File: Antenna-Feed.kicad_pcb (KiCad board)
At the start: 2 copper layers, 26 x 17.2 mm, 3 parts, among them J1 SMA, J2 SMA, J3 SMA

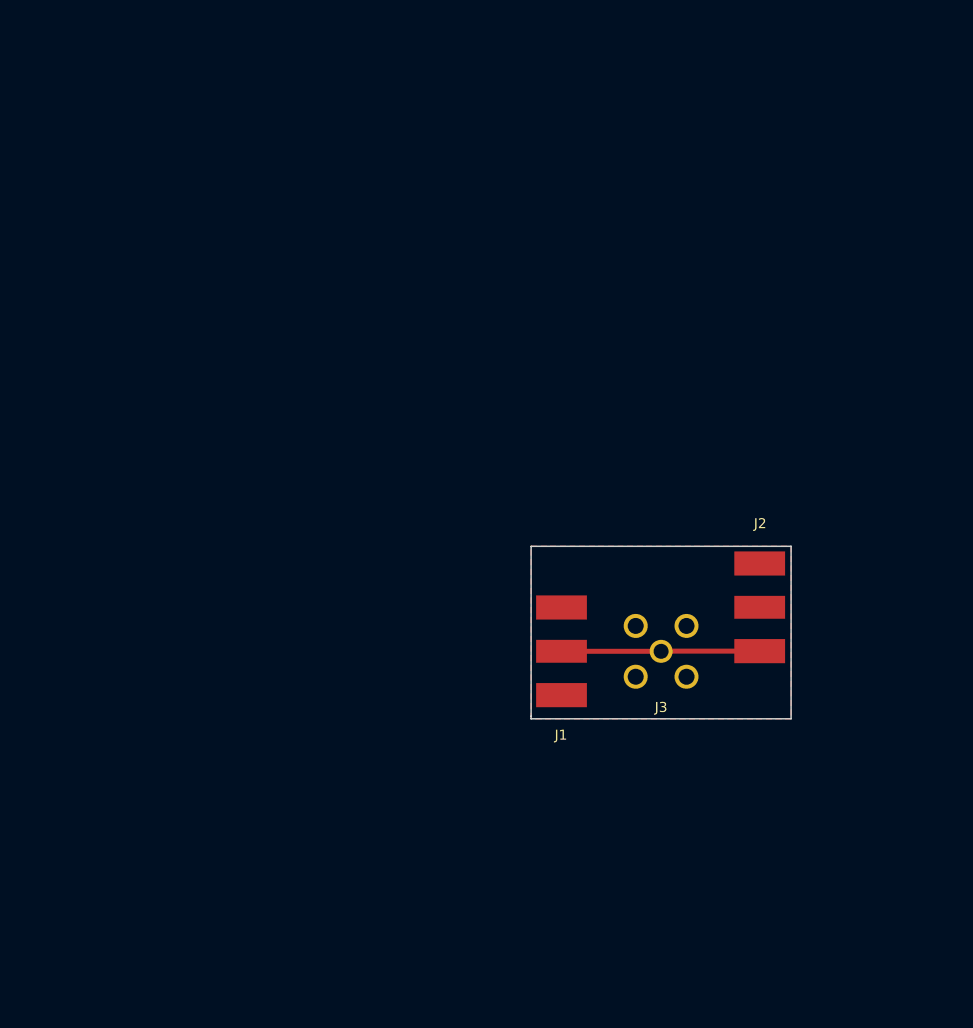
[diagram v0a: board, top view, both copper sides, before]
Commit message: initial revision conforming to Ana's structural model
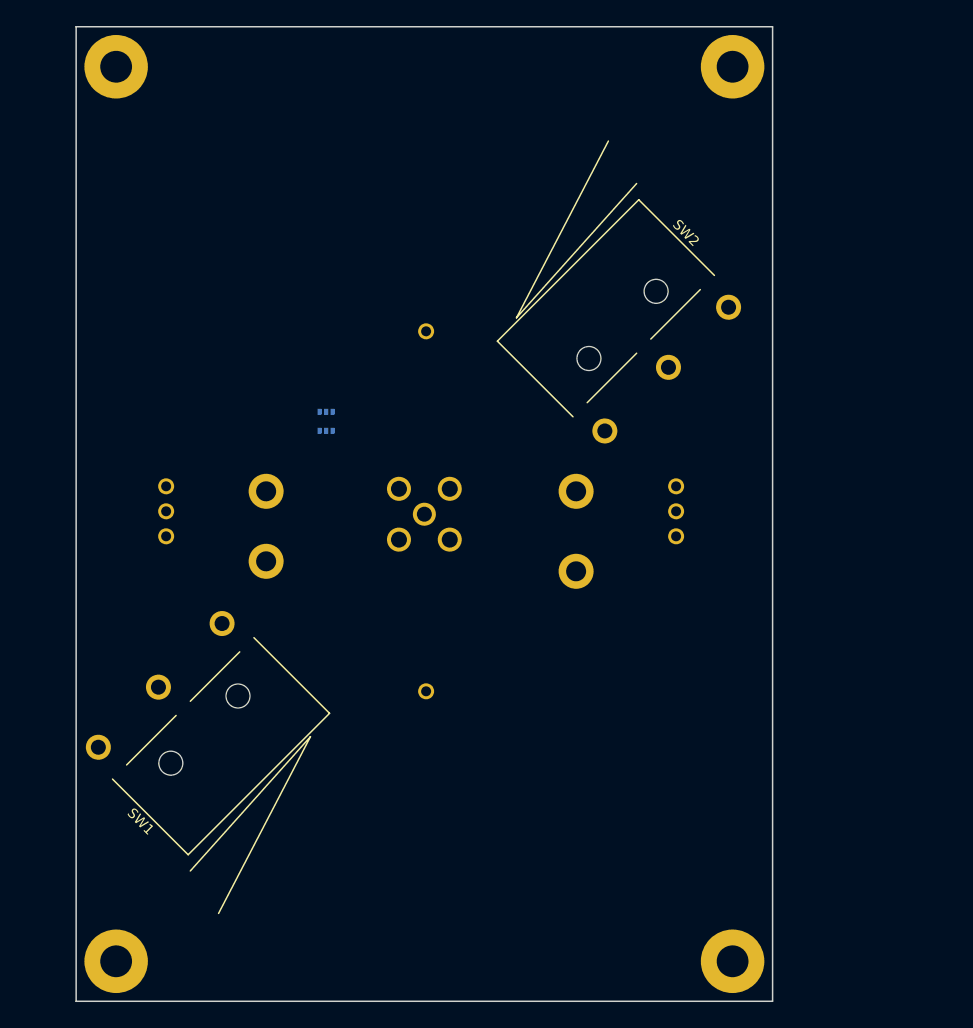
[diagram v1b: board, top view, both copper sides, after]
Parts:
- added J10: PC104PTH, SFUSat:PC104PTH, F.Cu at (155.7, 136.0)
- added J11: PC104PTH, SFUSat:PC104PTH, F.Cu at (94.0, 136.0)
- added J12: PC104PTH, SFUSat:PC104PTH, F.Cu at (94.0, 46.5)
- added J13: PC104PTH, SFUSat:PC104PTH, F.Cu at (155.7, 46.5)
- added J4: Conn_01x01, SFUSat:via-0.97mm, F.Cu at (125.0, 73.0)
- added J5: Conn_01x01, SFUSat:PTH-2.0mm, F.Cu at (109.0, 96.0)
- added J6: Conn_01x01, SFUSat:PTH-2.0mm, F.Cu at (109.0, 89.0)
- added J7: Conn_01x01, SFUSat:PTH-2.0mm, F.Cu at (140.0, 97.0)
- added J8: Conn_01x01, SFUSat:PTH-2.0mm, F.Cu at (140.0, 89.0)
- added J9: B3B-XH-A(LF)(SN), SFUSat:B3B-XH-A, B.Cu at (150.0, 91.0)
- added SW1: LIMIT_SWITCH, SFUSat:SS-3GLPD-R, F.Cu at (100.0, 110.0)
- added SW2: LIMIT_SWITCH, SFUSat:SS-3GLPD-R, F.Cu at (147.5, 75.2)
- added U1: NC7SZ157, SFUSat:SOT-363, B.Cu at (115.0, 82.0)
- J1: value SMA -> Conn_01x01; footprint SFUSat:SMA_EDGE -> SFUSat:via-0.97mm
- J2: value SMA -> B3B-XH-A(LF)(SN); footprint SFUSat:SMA_EDGE -> SFUSat:B3B-XH-A; moved to B.Cu
- J3: moved to B.Cu
- moved J2 62.6 mm to (99.0, 91.0), turned to 90 degrees
- moved J3 27.4 mm to (124.8, 91.3)
- moved J1 11.7 mm to (125.0, 109.0)
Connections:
- J2 pad 1: Net-(J1-Pad2) -> Net-(J2-Pad1)
- J2 pad 2: Net-(J1-Pad1) -> Net-(J2-Pad2)
- J3 pad 2: Net-(J1-Pad2) -> Net-(J3-Pad2)
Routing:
- net Net-(J1-Pad1): track 19.8 -> 0.00 mm
- removed copper zone on F.Cu, net Net-(J1-Pad2)
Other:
- board size 26 x 17.2 mm -> 69.7 x 97.5 mm

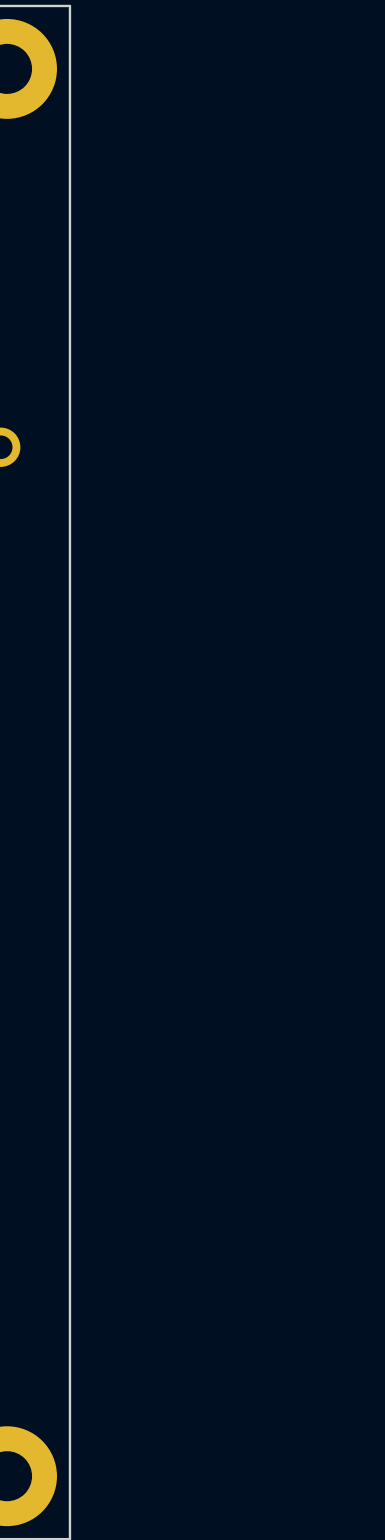
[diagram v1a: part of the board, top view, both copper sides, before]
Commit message: Added through holes to the right side of the antenna feed pcb
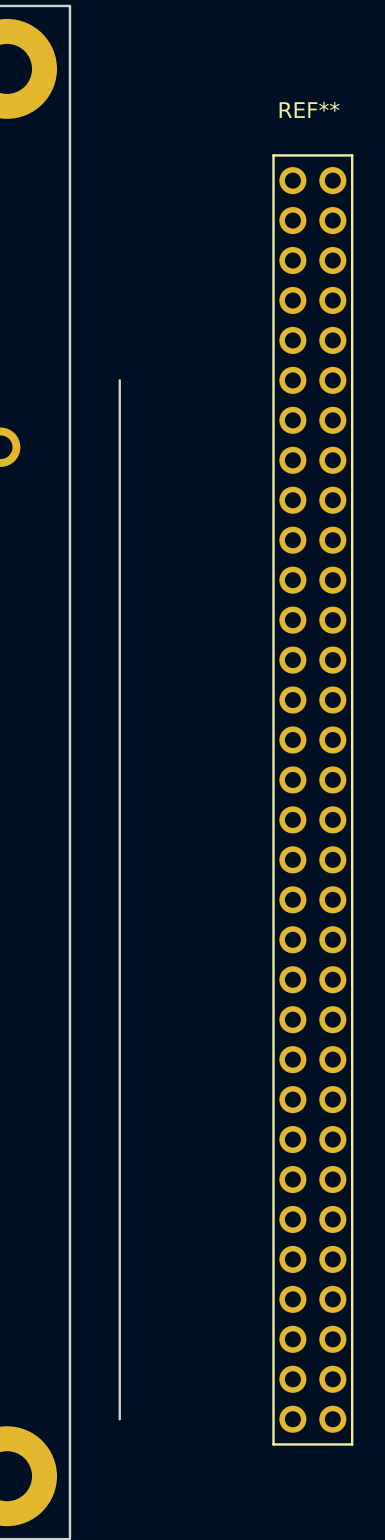
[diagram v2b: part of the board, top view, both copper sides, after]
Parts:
- added REF**: PC104-8bit, SFUSat:PC104-8bit, F.Cu at (175.1, 93.0)
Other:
- board size 69.7 x 97.5 mm -> 72.8 x 97.5 mm
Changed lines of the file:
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@@
-(kicad_pcb (version 4) (host pcbnew 4.0.7-e2-6376~58~ubuntu16.04.1)
+(kicad_pcb (version 4) (host pcbnew 4.0.7)
   (general
-    (links 17)
+    (links 0)
     (no_connects 17)
-    (area 89.924999 42.464999 159.725001 140.075001)
+    (area 80.650001 41.755 159.725001 144.700001)
     (thickness 1.6)
-    (drawings 6)
+    (drawings 7)
     (tracks 0)
     (zones 0)
-    (modules 16)
+    (modules 17)
     (nets 17)
   )
@@
       (net 7 "Net-(J9-Pad2)"))
   )
+  (module SFUSat:PC104-8bit (layer F.Cu)
+    (at 175.09 93.01)
+    (fp_text reference REF** (at -0.254 -43.815) (layer F.SilkS)
+      (effects (font (size 1 1) (thickness 0.15)))
+    )
+    (fp_text value PC104-8bit (at -0.127 -42.164) (layer F.Fab)
+      (effects (font (size 1 1) (thickness 0.15)))
+    )
+    (fp_line (start -2.5 40.97) (end 2.5 40.97) (layer F.SilkS) (width 0.15))
+    (fp_line (start -2.5 -40.97) (end -2.5 40.97) (layer F.SilkS) (width 0.15))
+    (fp_line (start 2.5 -40.97) (end 2.5 40.97) (layer F.SilkS) (width 0.15))
+    (fp_line (start -2.5 -40.97) (end 2.5 -40.97) (layer F.SilkS) (width 0.15))
+    (pad 32B thru_hole circle (at -1.27 -39.37) (size 1.72 1.72) (drill 1.02) (layers *.Cu *.Mask))
+    (pad 31B thru_hole circle (at -1.27 -36.83) (size 1.72 1.72) (drill 1.02) (layers *.Cu *.Mask))
+    (pad 30B thru_hole circle (at -1.27 -34.29) (size 1.72 1.72) (drill 1.02) (layers *.Cu *.Mask))
+    (pad 29B thru_hole circle (at -1.27 -31.75) (size 1.72 1.72) (drill 1.02) (layers *.Cu *.Mask))
+    (pad 28B thru_hole circle (at -1.27 -29.21) (size 1.72 1.72) (drill 1.02) (layers *.Cu *.Mask))
+    (pad 27B thru_hole circle (at -1.27 -26.67) (size 1.72 1.72) (drill 1.02) (layers *.Cu *.Mask))
+    (pad 26B thru_hole circle (at -1.27 -24.13) (size 1.72 1.72) (drill 1.02) (layers *.Cu *.Mask))
+    (pad 25B thru_hole circle (at -1.27 -21.59) (size 1.72 1.72) (drill 1.02) (layers *.Cu *.Mask))
+    (pad 24B thru_hole circle (at -1.27 -19.05) (size 1.72 1.72) (drill 1.02) (layers *.Cu *.Mask))
+    (pad 23B thru_hole circle (at -1.27 -16.51) (size 1.72 1.72) (drill 1.02) (layers *.Cu *.Mask))
+    (pad 22B thru_hole circle (at -1.27 -13.97) (size 1.72 1.72) (drill 1.02) (layers *.Cu *.Mask))
+    (pad 21B thru_hole circle (at -1.27 -11.43) (size 1.72 1.72) (drill 1.02) (layers *.Cu *.Mask))
+    (pad 20B thru_hole circle (at -1.27 -8.89) (size 1.72 1.72) (drill 1.02) (layers *.Cu *.Mask))
+    (pad 19B thru_hole circle (at -1.27 -6.35) (size 1.72 1.72) (drill 1.02) (layers *.Cu *.Mask))
+    (pad 18B thru_hole circle (at -1.27 -3.81) (size 1.72 1.72) (drill 1.02) (layers *.Cu *.Mask))
+    (pad 17B thru_hole circle (at -1.27 -1.27) (size 1.72 1.72) (drill 1.02) (layers *.Cu *.Mask))
+    (pad 16B thru_hole circle (at -1.27 1.27) (size 1.72 1.72) (drill 1.02) (layers *.Cu *.Mask))
+    (pad 15B thru_hole circle (at -1.27 3.81) (size 1.72 1.72) (drill 1.02) (layers *.Cu *.Mask))
+    (pad 14B thru_hole circle (at -1.27 6.35) (size 1.72 1.72) (drill 1.02) (layers *.Cu *.Mask))
+    (pad 13B thru_hole circle (at -1.27 8.89) (size 1.72 1.72) (drill 1.02) (layers *.Cu *.Mask))
+    (pad 12B thru_hole circle (at -1.27 11.43) (size 1.72 1.72) (drill 1.02) (layers *.Cu *.Mask))
+    (pad 11B thru_hole circle (at -1.27 13.97) (size 1.72 1.72) (drill 1.02) (layers *.Cu *.Mask))
+    (pad 10B thru_hole circle (at -1.27 16.51) (size 1.72 1.72) (drill 1.02) (layers *.Cu *.Mask))
+    (pad 9B thru_hole circle (at -1.27 19.05) (size 1.72 1.72) (drill 1.02) (layers *.Cu *.Mask))
+    (pad 8B thru_hole circle (at -1.27 21.59) (size 1.72 1.72) (drill 1.02) (layers *.Cu *.Mask))
+    (pad 7B thru_hole circle (at -1.27 24.13) (size 1.72 1.72) (drill 1.02) (layers *.Cu *.Mask))
+    (pad 6B thru_hole circle (at -1.27 26.67) (size 1.72 1.72) (drill 1.02) (layers *.Cu *.Mask))
+    (pad 5B thru_hole circle (at -1.27 29.21) (size 1.72 1.72) (drill 1.02) (layers *.Cu *.Mask))
+    (pad 4B thru_hole circle (at -1.27 31.75) (size 1.72 1.72) (drill 1.02) (layers *.Cu *.Mask))
+    (pad 3B thru_hole circle (at -1.27 34.29) (size 1.72 1.72) (drill 1.02) (layers *.Cu *.Mask))
+    (pad 2B thru_hole circle (at -1.27 36.83) (size 1.72 1.72) (drill 1.02) (layers *.Cu *.Mask))
+    (pad 1B thru_hole circle (at -1.27 39.37) (size 1.72 1.72) (drill 1.02) (layers *.Cu *.Mask))
+    (pad 32A thru_hole circle (at 1.27 -39.37) (size 1.72 1.72) (drill 1.02) (layers *.Cu *.Mask))
+    (pad 31A thru_hole circle (at 1.27 -36.83) (size 1.72 1.72) (drill 1.02) (layers *.Cu *.Mask))
+    (pad 30A thru_hole circle (at 1.27 -34.29) (size 1.72 1.72) (drill 1.02) (layers *.Cu *.Mask))
+    (pad 29A thru_hole circle (at 1.27 -31.75) (size 1.72 1.72) (drill 1.02) (layers *.Cu *.Mask))
+    (pad 28A thru_hole circle (at 1.27 -29.21) (size 1.72 1.72) (drill 1.02) (layers *.Cu *.Mask))
+    (pad 27A thru_hole circle (at 1.27 -26.67) (size 1.72 1.72) (drill 1.02) (layers *.Cu *.Mask))
+    (pad 26A thru_hole circle (at 1.27 -24.13) (size 1.72 1.72) (drill 1.02) (layers *.Cu *.Mask))
+    (pad 25A thru_hole circle (at 1.27 -21.59) (size 1.72 1.72) (drill 1.02) (layers *.Cu *.Mask))
+    (pad 24A thru_hole circle (at 1.27 -19.05) (size 1.72 1.72) (drill 1.02) (layers *.Cu *.Mask))
+    (pad 23A thru_hole circle (at 1.27 -16.51) (size 1.72 1.72) (drill 1.02) (layers *.Cu *.Mask))
+    (pad 22A thru_hole circle (at 1.27 -13.97) (size 1.72 1.72) (drill 1.02) (layers *.Cu *.Mask))
+    (pad 21A thru_hole circle (at 1.27 -11.43) (size 1.72 1.72) (drill 1.02) (layers *.Cu *.Mask))
+    (pad 20A thru_hole circle (at 1.27 -8.89) (size 1.72 1.72) (drill 1.02) (layers *.Cu *.Mask))
+    (pad 19A thru_hole circle (at 1.27 -6.35) (size 1.72 1.72) (drill 1.02) (layers *.Cu *.Mask))
+    (pad 18A thru_hole circle (at 1.27 -3.81) (size 1.72 1.72) (drill 1.02) (layers *.Cu *.Mask))
+    (pad 17A thru_hole circle (at 1.27 -1.27) (size 1.72 1.72) (drill 1.02) (layers *.Cu *.Mask))
+    (pad 16A thru_hole circle (at 1.27 1.27) (size 1.72 1.72) (drill 1.02) (layers *.Cu *.Mask))
+    (pad 15A thru_hole circle (at 1.27 3.81) (size 1.72 1.72) (drill 1.02) (layers *.Cu *.Mask))
+    (pad 14A thru_hole circle (at 1.27 6.35) (size 1.72 1.72) (drill 1.02) (layers *.Cu *.Mask))
+    (pad 13A thru_hole circle (at 1.27 8.89) (size 1.72 1.72) (drill 1.02) (layers *.Cu *.Mask))
+    (pad 12A thru_hole circle (at 1.27 11.43) (size 1.72 1.72) (drill 1.02) (layers *.Cu *.Mask))
+    (pad 11A thru_hole circle (at 1.27 13.97) (size 1.72 1.72) (drill 1.02) (layers *.Cu *.Mask))
+    (pad 10A thru_hole circle (at 1.27 16.51) (size 1.72 1.72) (drill 1.02) (layers *.Cu *.Mask))
+    (pad 9A thru_hole circle (at 1.27 19.05) (size 1.72 1.72) (drill 1.02) (layers *.Cu *.Mask))
+    (pad 8A thru_hole circle (at 1.27 21.59) (size 1.72 1.72) (drill 1.02) (layers *.Cu *.Mask))
+    (pad 7A thru_hole circle (at 1.27 24.13) (size 1.72 1.72) (drill 1.02) (layers *.Cu *.Mask))
+    (pad 6A thru_hole circle (at 1.27 26.67) (size 1.72 1.72) (drill 1.02) (layers *.Cu *.Mask))
+    (pad 5A thru_hole circle (at 1.27 29.21) (size 1.72 1.72) (drill 1.02) (layers *.Cu *.Mask))
+    (pad 4A thru_hole circle (at 1.27 31.75) (size 1.72 1.72) (drill 1.02) (layers *.Cu *.Mask))
+    (pad 3A thru_hole circle (at 1.27 34.29) (size 1.72 1.72) (drill 1.02) (layers *.Cu *.Mask))
+    (pad 2A thru_hole circle (at 1.27 36.83) (size 1.72 1.72) (drill 1.02) (layers *.Cu *.Mask))
+    (pad 1A thru_hole circle (at 1.27 39.37) (size 1.72 1.72) (drill 1.02) (layers *.Cu *.Mask))
+  )
+  (gr_line (start 162.815 132.38) (end 162.815 66.34) (layer Edge.Cuts) (width 0.15))
   (gr_line (start 159.65 140) (end 159.65 42.54) (layer Edge.Cuts) (width 0.15))
   (dimension 97.5 (width 0.3) (layer Dwgs.User)

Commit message: I forgot to save before the last push
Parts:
- removed REF**: PC104-8bit, SFUSat:PC104-8bit
- added U1: B3B-XH-A-AntennaFeed-DC(LF)(SN), SFUSat:B3B-XH-A-AntennaFeed-DC, B.Cu at (160.3, 132.4)
- added U1: B3B-XH-A-AntennaFeed-RFDep(LF)(SN), SFUSat:B3B-XH-A-AntennaFeed-RFDep, B.Cu at (160.3, 117.1)
- added U1: B3B-XH-A-AntennaFeed-DepPow(LF)(SN), SFUSat:B3B-XH-A-AntennaFeed-DepPow, B.Cu at (162.8, 74.0)
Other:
- board size 72.8 x 97.5 mm -> 74.9 x 97.5 mm

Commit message: placed switches in accordance to latest structural model
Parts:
- moved SW1 40.0 mm to (140.0, 109.2), turned to 125.5 degrees
- moved SW2 37.3 mm to (110.2, 72.8), turned to 305 degrees
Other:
- outline, holes or cut-outs redrawn
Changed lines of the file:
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@@
-(kicad_pcb (version 4) (host pcbnew 4.0.7)
+(kicad_pcb (version 4) (host pcbnew 4.0.7-e2-6376~58~ubuntu16.04.1)
   (general
-    (links 0)
+    (links 17)
     (no_connects 17)
-    (area 80.650001 41.755 179.663 144.700001)
+    (area 89.924999 42.464999 165.005001 140.075001)
     (thickness 1.6)
-    (drawings 18)
+    (drawings 22)
     (tracks 0)
     (zones 0)
@@
   )
   (module SFUSat:SS-3GLPD-R (layer F.Cu)
-    (at 100 110 225)
-    (fp_text reference SW1 (at 11 -6 315) (layer F.SilkS)
-      (effects (font (size 1 1) (thickness 0.15)))
-    )
-    (fp_text value LIMIT_SWITCH (at 0 -8 225) (layer F.Fab)
+    (at 140.02 109.16 125.5)
+    (fp_text reference SW1 (at 11 -6 215.5) (layer F.SilkS)
+      (effects (font (size 1 1) (thickness 0.15)))
+    )
+    (fp_text value LIMIT_SWITCH (at 0 -8 125.5) (layer F.Fab)
       (effects (font (size 1 1) (thickness 0.15)))
     )
@@
     (fp_line (start -8 -1) (end -1 -1) (layer F.SilkS) (width 0.15))
     (fp_line (start -10 -1) (end -10 -11.7) (layer F.SilkS) (width 0.15))
-    (pad NO thru_hole circle (at 0.25 2.25 225) (size 2.5 2.5) (drill 1.5) (layers *.Cu *.Mask)
+    (pad NO thru_hole circle (at 0.25 2.25 125.5) (size 2.5 2.5) (drill 1.5) (layers *.Cu *.Mask)
       (net 5 "Net-(SW1-PadNO)"))
-    (pad COM thru_hole circle (at -8.75 2.25 225) (size 2.5 2.5) (drill 1.5) (layers *.Cu *.Mask)
+    (pad COM thru_hole circle (at -8.75 2.25 125.5) (size 2.5 2.5) (drill 1.5) (layers *.Cu *.Mask)
       (net 13 "Net-(J9-Pad1)"))
-    (pad NC thru_hole circle (at 8.75 2.25 225) (size 2.5 2.5) (drill 1.5) (layers *.Cu *.Mask)
+    (pad NC thru_hole circle (at 8.75 2.25 125.5) (size 2.5 2.5) (drill 1.5) (layers *.Cu *.Mask)
       (net 15 "Net-(SW1-PadNC)"))
-    (pad "" np_thru_hole circle (at 4.75 -4 225) (size 2.4 2.4) (drill 2.4) (layers *.Cu *.Mask))
-    (pad "" np_thru_hole circle (at -4.75 -4 225) (size 2.4 2.4) (drill 2.4) (layers *.Cu *.Mask))
+    (pad "" np_thru_hole circle (at 4.75 -4 125.5) (size 2.4 2.4) (drill 2.4) (layers *.Cu *.Mask))
+    (pad "" np_thru_hole circle (at -4.75 -4 125.5) (size 2.4 2.4) (drill 2.4) (layers *.Cu *.Mask))
     (model /home/tobi/Cubesat/z-panel/KiCad-Lib/SFUSat.pretty/SS_3GLP_R.wrl
       (at (xyz 0 0 0))
@@
   )
   (module SFUSat:SS-3GLPD-R (layer F.Cu)
-    (at 147.46967 75.187184 45)
-    (fp_text reference SW2 (at 11 -6 135) (layer F.SilkS)
-      (effects (font (size 1 1) (thickness 0.15)))
-    )
-    (fp_text value LIMIT_SWITCH (at 0 -8 45) (layer F.Fab)
+    (at 110.218904 72.77 305)
+    (fp_text reference SW2 (at 11 -6 395) (layer F.SilkS)
+      (effects (font (size 1 1) (thickness 0.15)))
+    )
+    (fp_text value LIMIT_SWITCH (at 0 -8 305) (layer F.Fab)
       (effects (font (size 1 1) (thickness 0.15)))
     )
@@
     (fp_line (start -8 -1) (end -1 -1) (layer F.SilkS) (width 0.15))
     (fp_line (start -10 -1) (end -10 -11.7) (layer F.SilkS) (width 0.15))
-    (pad NO thru_hole circle (at 0.25 2.25 45) (size 2.5 2.5) (drill 1.5) (layers *.Cu *.Mask)
+    (pad NO thru_hole circle (at 0.25 2.25 305) (size 2.5 2.5) (drill 1.5) (layers *.Cu *.Mask)
       (net 6 "Net-(SW2-PadNO)"))
-    (pad COM thru_hole circle (at -8.75 2.25 45) (size 2.5 2.5) (drill 1.5) (layers *.Cu *.Mask)
+    (pad COM thru_hole circle (at -8.75 2.25 305) (size 2.5 2.5) (drill 1.5) (layers *.Cu *.Mask)
       (net 13 "Net-(J9-Pad1)"))
-    (pad NC thru_hole circle (at 8.75 2.25 45) (size 2.5 2.5) (drill 1.5) (layers *.Cu *.Mask)
+    (pad NC thru_hole circle (at 8.75 2.25 305) (size 2.5 2.5) (drill 1.5) (layers *.Cu *.Mask)
       (net 16 "Net-(SW2-PadNC)"))
-    (pad "" np_thru_hole circle (at 4.75 -4 45) (size 2.4 2.4) (drill 2.4) (layers *.Cu *.Mask))
-    (pad "" np_thru_hole circle (at -4.75 -4 45) (size 2.4 2.4) (drill 2.4) (layers *.Cu *.Mask))
+    (pad "" np_thru_hole circle (at 4.75 -4 305) (size 2.4 2.4) (drill 2.4) (layers *.Cu *.Mask))
+    (pad "" np_thru_hole circle (at -4.75 -4 305) (size 2.4 2.4) (drill 2.4) (layers *.Cu *.Mask))
     (model /home/tobi/Cubesat/z-panel/KiCad-Lib/SFUSat.pretty/SS_3GLP_R.wrl
       (at (xyz 0 0 0))
@@
     (pad 26A thru_hole circle (at 5.08 0 90) (size 1.6 1.6) (drill 1) (layers *.Cu *.Mask))
   )
-  (gr_line (start 159.66 63.8) (end 159.66 43.48) (layer Edge.Cuts) (width 0.15))
+  (gr_circle (center 116.25 74.38) (end 116.33 74.38) (layer F.SilkS) (width 0.2))
+  (gr_circle (center 110.86 66.7) (end 110.95 66.7) (layer F.SilkS) (width 0.2))
+  (gr_circle (center 134.01 107.79) (end 134.05 107.79) (layer F.SilkS) (width 0.2))
+  (gr_circle (center 139.53 115.4) (end 139.54 115.4) (layer F.SilkS) (width 1))
+  (gr_line (start 159.66 63.8) (end 159.66 42.54) (layer Edge.Cuts) (width 0.15))
   (gr_line (start 164.93 63.8) (end 159.66 63.8) (layer Edge.Cuts) (width 0.15))
   (gr_line (start 164.93 76.5) (end 164.93 63.8) (layer Edge.Cuts) (width 0.15))
@@
   (gr_line (start 162.39 134.92) (end 162.39 124.76) (layer Edge.Cuts) (width 0.15))
   (gr_line (start 159.66 134.92) (end 162.39 134.92) (layer Edge.Cuts) (width 0.15))
-  (gr_line (start 159.66 140) (end 159.66 135) (layer Edge.Cuts) (width 0.15))
+  (gr_line (start 159.66 140) (end 159.66 134.92) (layer Edge.Cuts) (width 0.15))
   (dimension 97.5 (width 0.3) (layer Dwgs.User)
     (gr_text "97.500 mm" (at 87.15 91.25 90) (layer Dwgs.User)
@@
     (arrow2b (pts (xy 88.5 140) (xy 87.913579 138.873496)))
   )
-  (gr_line (start 90 42.54) (end 159.65 42.54) (layer Edge.Cuts) (width 0.15))
+  (gr_line (start 90 42.54) (end 159.66 42.54) (layer Edge.Cuts) (width 0.15))
   (dimension 69.7 (width 0.3) (layer Dwgs.User)
     (gr_text "69.700 mm" (at 124.85 143.35) (layer Dwgs.User)
@@
     (arrow2b (pts (xy 90 142) (xy 91.126504 141.413579)))
   )
-  (gr_line (start 90 140) (end 159.65 140) (layer Edge.Cuts) (width 0.15))
+  (gr_line (start 90 140) (end 159.66 140) (layer Edge.Cuts) (width 0.15))
   (gr_line (start 90 140) (end 90 42.54) (layer Edge.Cuts) (width 0.15))
 )
